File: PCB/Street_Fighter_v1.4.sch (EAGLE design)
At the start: 76 parts, among them J1 FEMALE 2x3, Q1 BSS138, Q10 BSS138, Q2 BSS138, Q3 FQP30N06L, Q4 BSS138, Q5 BSS138, Q6 BSS138, Q7 BSS138, Q9 BSS138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

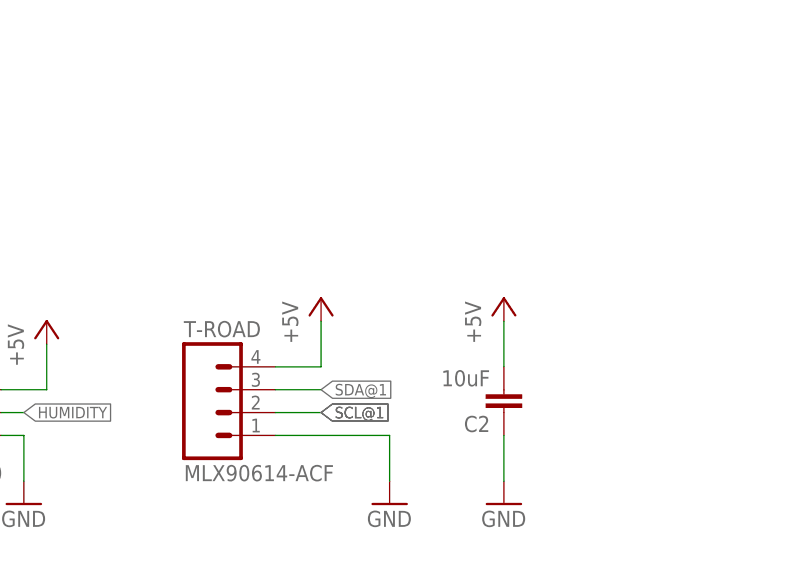
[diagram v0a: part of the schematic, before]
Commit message: Updated mounting plate for traffic sensors. Also started adding in the possibility for more than 2 PIR sensors.
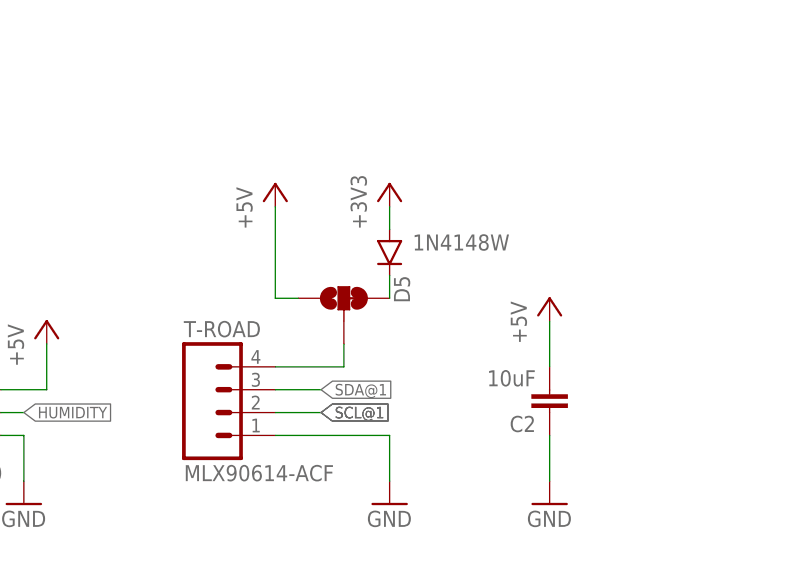
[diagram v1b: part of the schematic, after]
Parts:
- added D5: 1N4148W, SparkFun-DiscreteSemi:DIODESOD123
- added XBEE-OUT1: JUMPER-PAD-3-2OF3_NC_BY_TRACE_SMALL, SparkFun-Passives:JUMPER-PAD-3-2OF3_NC_BY_TRACE_SMALL
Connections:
- new net N$7: D5.C, XBEE-OUT1.3
- new net N$8: T-ROAD.4, XBEE-OUT1.2
- net +3V3: now also D5.A
- net +5V: now also XBEE-OUT1.1; no longer T-ROAD.4
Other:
- moved on the sheet: C2
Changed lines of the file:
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@@
 <part name="GND12" library="supply1" deviceset="GND" device=""/>
 <part name="T-ROAD" library="SparkFun-Connectors" deviceset="M04" device="PTH" value="MLX90614-ACF"/>
-<part name="P+14" library="supply1" deviceset="+5V" device=""/>
 <part name="GND13" library="supply1" deviceset="GND" device=""/>
 <part name="P+18" library="supply1" deviceset="+5V" device=""/>
@@
 <part name="R31" library="SparkFun-Passives" deviceset="RESISTOR" device="1206" value="4.7K"/>
 <part name="R32" library="SparkFun-Passives" deviceset="RESISTOR" device="1206" value="4.7K"/>
+<part name="+3V14" library="supply1" deviceset="+3V3" device=""/>
+<part name="XBEE-OUT1" library="SparkFun-Passives" deviceset="JUMPER-PAD-3-2OF3_NC_BY_TRACE" device="_SMALL"/>
+<part name="P+14" library="supply1" deviceset="+5V" device=""/>
+<part name="D5" library="SparkFun-DiscreteSemi" deviceset="DIODE" device="SOD123" value="1N4148W"/>
 </parts>
 <sheets>
@@
 <wire x1="254" y1="144.78" x2="254" y2="195.58" width="0.8128" layer="97"/>
 <wire x1="254" y1="195.58" x2="335.28" y2="195.58" width="0.8128" layer="97"/>
-<wire x1="294.64" y1="78.74" x2="337.82" y2="78.74" width="0.4064" layer="114"/>
-<wire x1="337.82" y1="78.74" x2="337.82" y2="43.18" width="0.4064" layer="114"/>
-<wire x1="337.82" y1="43.18" x2="294.64" y2="43.18" width="0.4064" layer="114"/>
-<wire x1="294.64" y1="43.18" x2="294.64" y2="78.74" width="0.4064" layer="114"/>
+<wire x1="294.64" y1="93.98" x2="342.9" y2="93.98" width="0.4064" layer="114"/>
+<wire x1="342.9" y1="93.98" x2="342.9" y2="43.18" width="0.4064" layer="114"/>
+<wire x1="342.9" y1="43.18" x2="294.64" y2="43.18" width="0.4064" layer="114"/>
+<wire x1="294.64" y1="43.18" x2="294.64" y2="93.98" width="0.4064" layer="114"/>
 <wire x1="7.62" y1="73.66" x2="76.2" y2="73.66" width="0.4064" layer="115"/>
 <wire x1="76.2" y1="73.66" x2="76.2" y2="43.18" width="0.4064" layer="115"/>
@@
 <instance part="GND12" gate="1" x="325.12" y="149.86"/>
 <instance part="T-ROAD" gate="G$1" x="302.26" y="60.96"/>
-<instance part="P+14" gate="1" x="312.42" y="73.66"/>
 <instance part="GND13" gate="1" x="320.04" y="50.8"/>
 <instance part="P+18" gate="1" x="71.12" y="71.12"/>
@@
 <instance part="P+26" gate="1" x="274.32" y="190.5"/>
 <instance part="P+16" gate="1" x="187.96" y="73.66"/>
-<instance part="P+4" gate="1" x="332.74" y="73.66"/>
-<instance part="GND3" gate="1" x="332.74" y="50.8"/>
-<instance part="C2" gate="G$1" x="332.74" y="63.5" rot="R180"/>
+<instance part="P+4" gate="1" x="337.82" y="73.66"/>
+<instance part="GND3" gate="1" x="337.82" y="50.8"/>
+<instance part="C2" gate="G$1" x="337.82" y="63.5" rot="R180"/>
 <instance part="DS18B20" gate="G$1" x="228.6" y="58.42"/>
 <instance part="P+17" gate="1" x="218.44" y="139.7"/>
@@
 <instance part="R31" gate="G$1" x="447.04" y="66.04" rot="R90"/>
 <instance part="R32" gate="G$1" x="482.6" y="60.96" rot="R90"/>
+<instance part="+3V14" gate="G$1" x="320.04" y="86.36"/>
+<instance part="XBEE-OUT1" gate="G$1" x="314.96" y="73.66" smashed="yes" rot="R90"/>
+<instance part="P+14" gate="1" x="307.34" y="86.36"/>
+<instance part="D5" gate="G$1" x="320.04" y="78.74" smashed="yes" rot="R270">
+<attribute name="NAME" x="320.5226" y="76.2" size="1.778" layer="95" rot="R270"/>
+<attribute name="VALUE" x="322.58" y="78.9686" size="1.778" layer="96"/>
+</instance>
 </instances>
 <busses>
@@
 <wire x1="20.32" y1="63.5" x2="25.4" y2="63.5" width="0.2032" layer="91"/>
 <wire x1="25.4" y1="63.5" x2="25.4" y2="68.58" width="0.2032" layer="91"/>
-</segment>
-<segment>
-<pinref part="T-ROAD" gate="G$1" pin="4"/>
-<wire x1="307.34" y1="66.04" x2="312.42" y2="66.04" width="0.2032" layer="91"/>
-<wire x1="312.42" y1="66.04" x2="312.42" y2="71.12" width="0.2032" layer="91"/>
-<pinref part="P+14" gate="1" pin="+5V"/>
 </segment>
 <segment>
@@
 <pinref part="P+4" gate="1" pin="+5V"/>
 <pinref part="C2" gate="G$1" pin="2"/>
-<wire x1="332.74" y1="71.12" x2="332.74" y2="66.04" width="0.1524" layer="91"/>
+<wire x1="337.82" y1="71.12" x2="337.82" y2="66.04" width="0.1524" layer="91"/>
 </segment>
 <segment>
@@
 <wire x1="447.04" y1="71.12" x2="441.96" y2="71.12" width="0.2032" layer="91"/>
 <junction x="441.96" y="71.12"/>
+</segment>
+<segment>
+<pinref part="P+14" gate="1" pin="+5V"/>
+<wire x1="307.34" y1="83.82" x2="307.34" y2="73.66" width="0.2032" layer="91"/>
+<pinref part="XBEE-OUT1" gate="G$1" pin="1"/>
+<wire x1="307.34" y1="73.66" x2="309.88" y2="73.66" width="0.2032" layer="91"/>
 </segment>
 </net>
@@
 <pinref part="+3V10" gate="G$1" pin="+3V3"/>
 </segment>
+<segment>
+<pinref part="+3V14" gate="G$1" pin="+3V3"/>
+<pinref part="D5" gate="G$1" pin="A"/>
+<wire x1="320.04" y1="83.82" x2="320.04" y2="81.28" width="0.2032" layer="91"/>
+</segment>
 </net>
 <net name="V+" class="0">
@@
 <pinref part="C2" gate="G$1" pin="1"/>
 <pinref part="GND3" gate="1" pin="GND"/>
-<wire x1="332.74" y1="53.34" x2="332.74" y2="58.42" width="0.1524" layer="91"/>
+<wire x1="337.82" y1="53.34" x2="337.82" y2="58.42" width="0.1524" layer="91"/>
 </segment>
 <segment>
@@
 </segment>
 </net>
+<net name="N$8" class="0">
+<segment>
+<pinref part="T-ROAD" gate="G$1" pin="4"/>
+<wire x1="307.34" y1="66.04" x2="314.96" y2="66.04" width="0.2032" layer="91"/>
+<wire x1="314.96" y1="66.04" x2="314.96" y2="68.58" width="0.2032" layer="91"/>
+<pinref part="XBEE-OUT1" gate="G$1" pin="2"/>
+</segment>
+</net>
+<net name="N$7" class="0">
+<segment>
+<pinref part="XBEE-OUT1" gate="G$1" pin="3"/>
+<pinref part="D5" gate="G$1" pin="C"/>
+<wire x1="320.04" y1="73.66" x2="320.04" y2="76.2" width="0.2032" layer="91"/>
+</segment>
+</net>
